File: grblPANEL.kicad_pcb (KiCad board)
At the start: 4 copper layers, 84 x 55 mm, 122 parts, among them J101 Conn_01x02, J201 2x5x1.27mm, J202 USB_C_Receptacle_USB2.0, J301 Conn_01x02, J401 Conn_01x02, J501 ILI9488, J601 Conn_02x10_Odd_Even, J701 Conn_01x04, J702 Conn_01x04, J703 Conn_01x04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

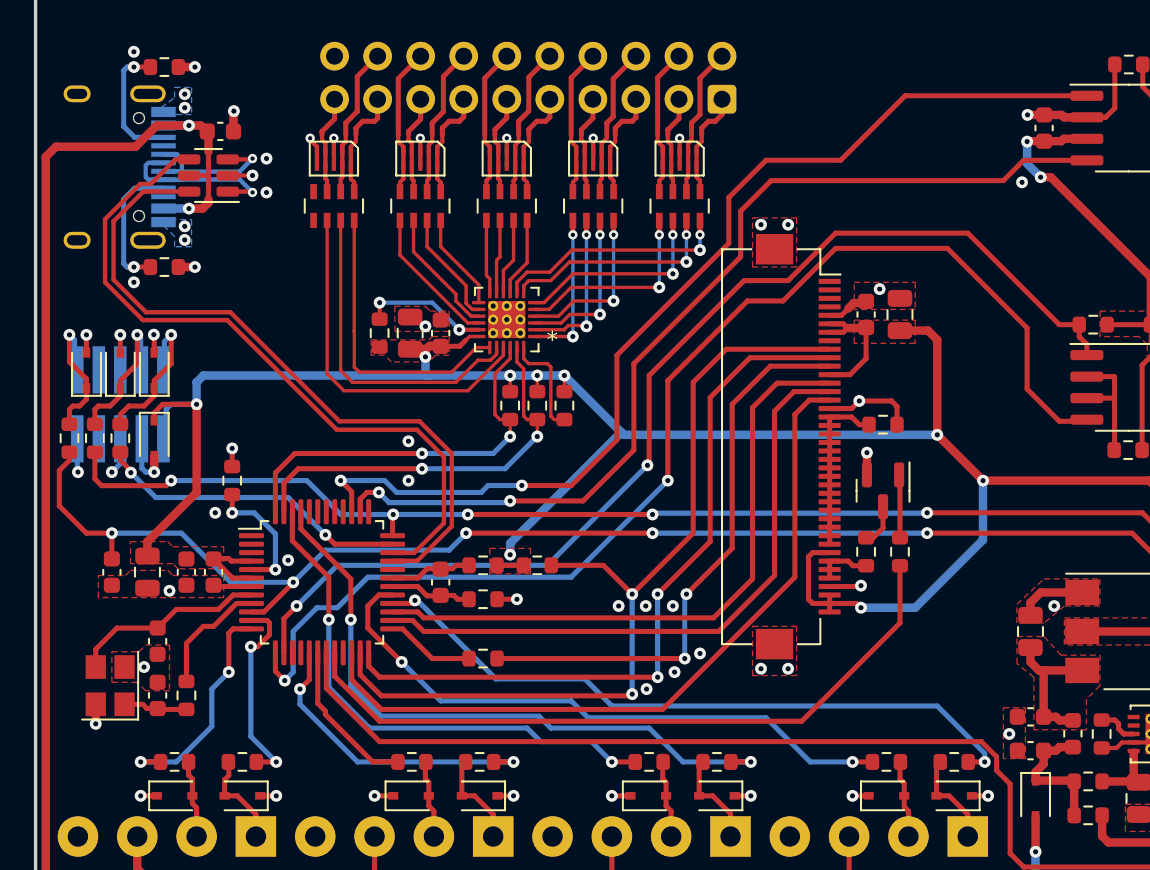
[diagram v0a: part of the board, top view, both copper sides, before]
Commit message: Ensure silkscreen is not covering holes
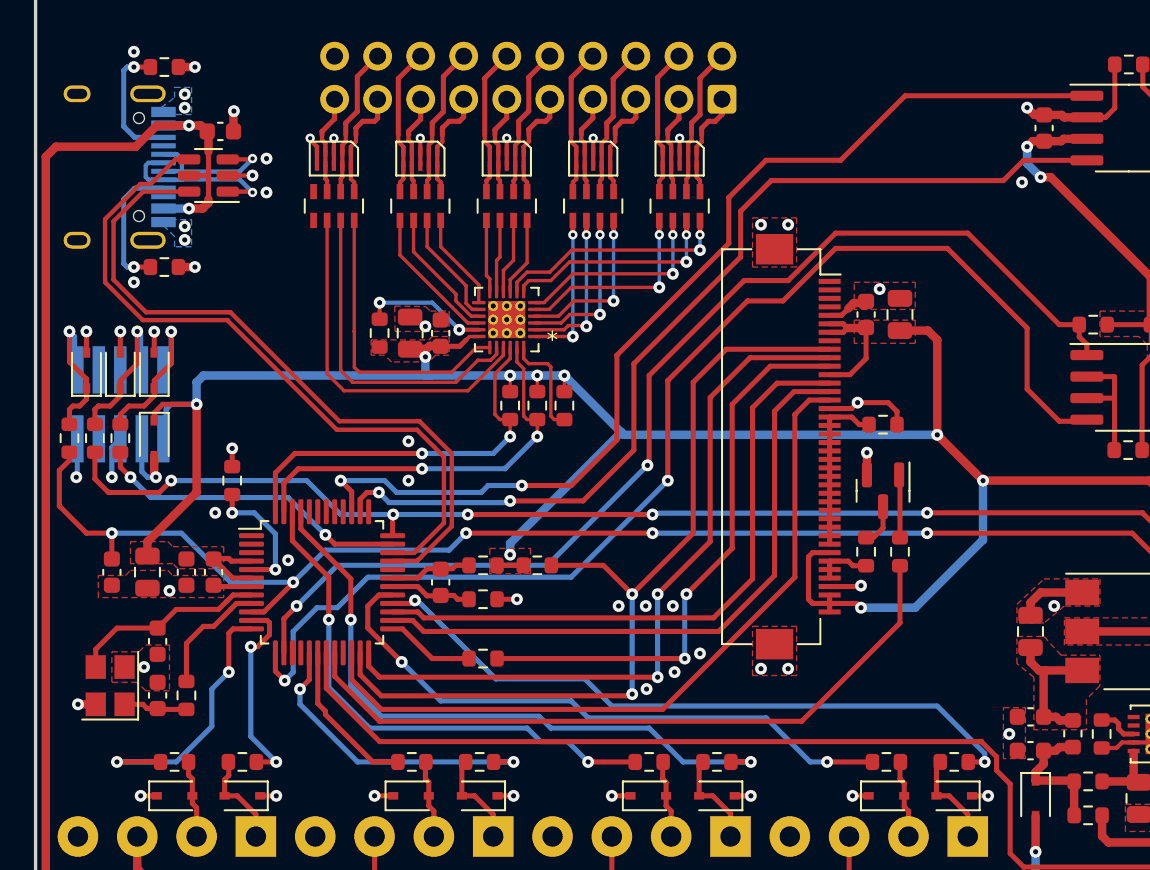
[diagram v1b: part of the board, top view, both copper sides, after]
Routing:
- net ENCODER_4_B: track 13.6 -> 16.4 mm
- net GND: track 91.8 -> 93.6 mm

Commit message: small cleanups
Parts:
- RN601, RN602, RN603, RN604, RN605: footprint Resistor_SMD:R_Array_Concave_4x0603 -> Resistor_SMD:R_Array_Convex_4x0603
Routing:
- net GND: track 93.6 -> 92.8 mm

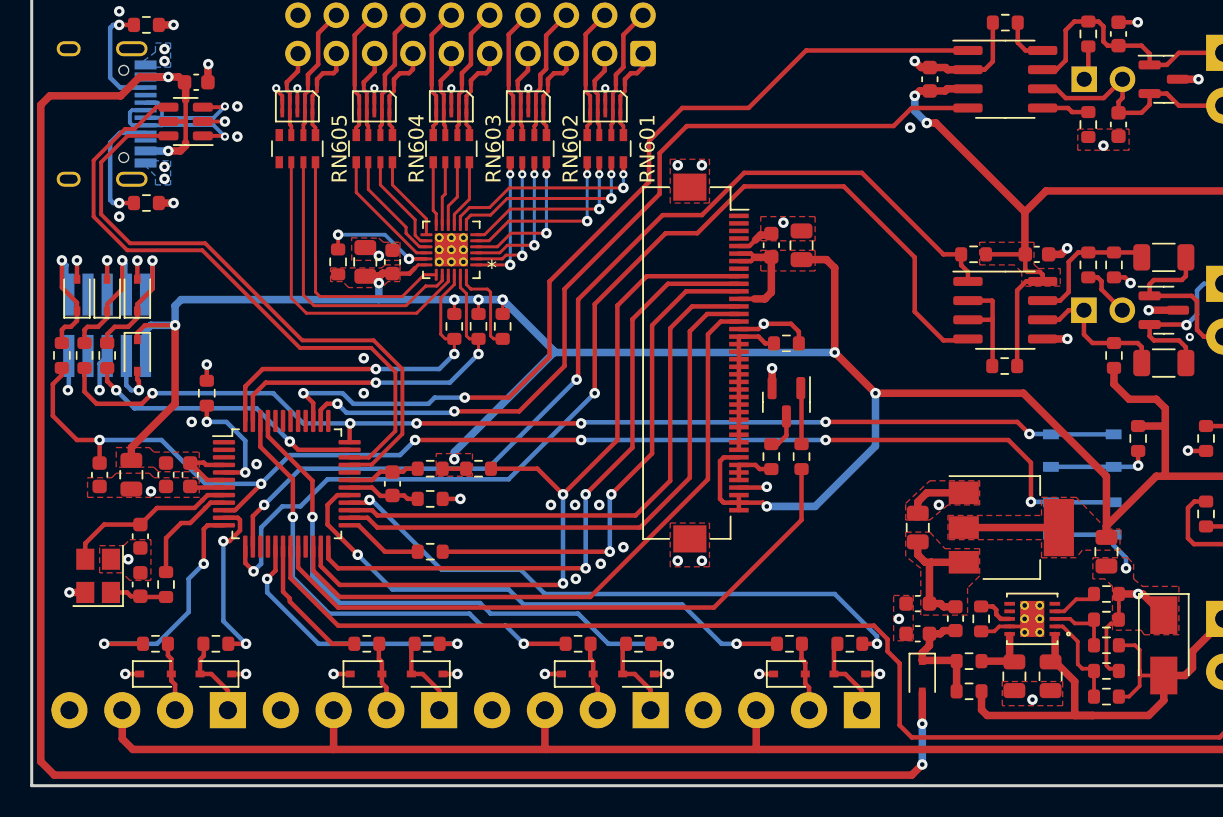
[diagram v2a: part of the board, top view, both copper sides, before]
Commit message: place gnd vias near all signal and power vias
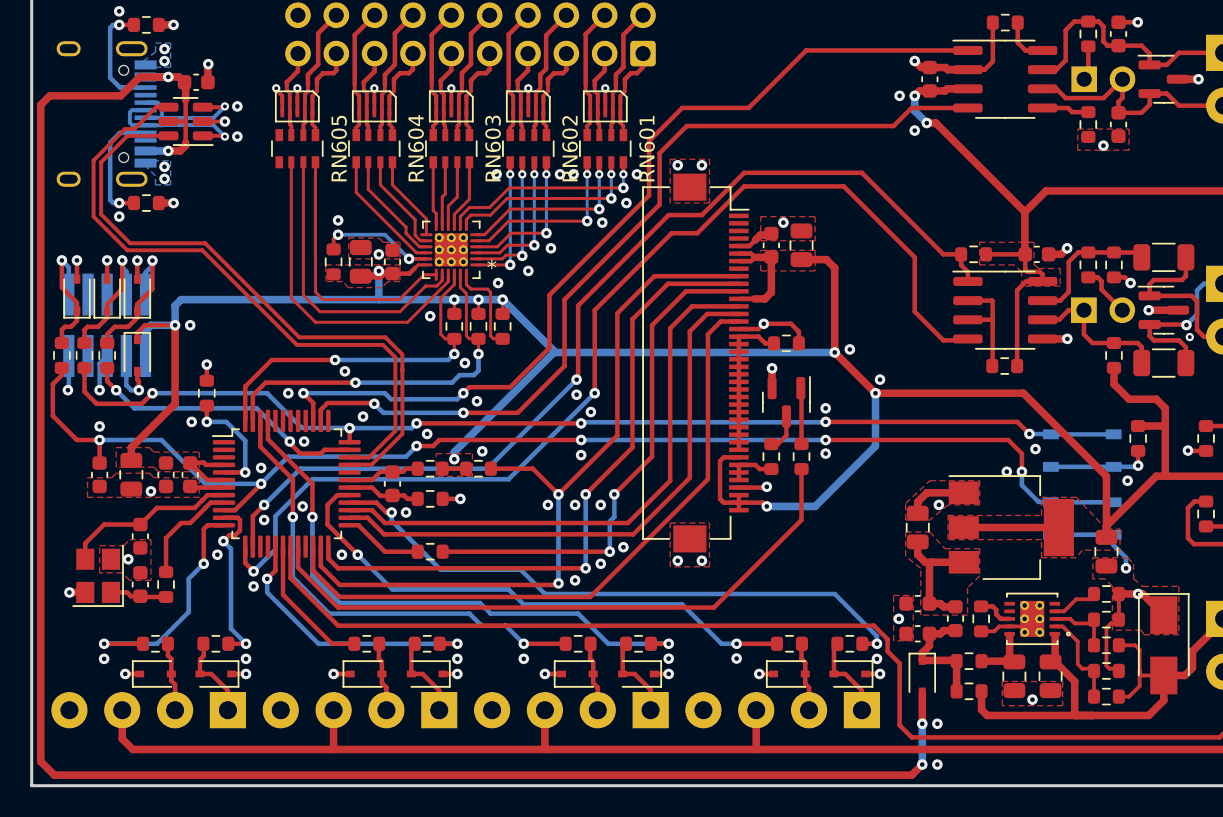
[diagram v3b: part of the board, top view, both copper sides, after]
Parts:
- moved C601 0.30 mm to (42.8, 149.3)
- moved R604 0.30 mm to (41.0, 149.3)
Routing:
- net +3V3: track 354.5 -> 355.3 mm
- net DISPLAY_CS: track 52.1 -> 51.4 mm
- net /MCU/USB_D-: track 41.5 -> 42.2 mm
- net KEYPAD_CLK: track 23.9 -> 24.5 mm
- net CAN_TX: track 60.6 -> 60.0 mm
- net /MCU/USB_D+: track 42.1 -> 42.6 mm
- net GND: vias 72 -> 117

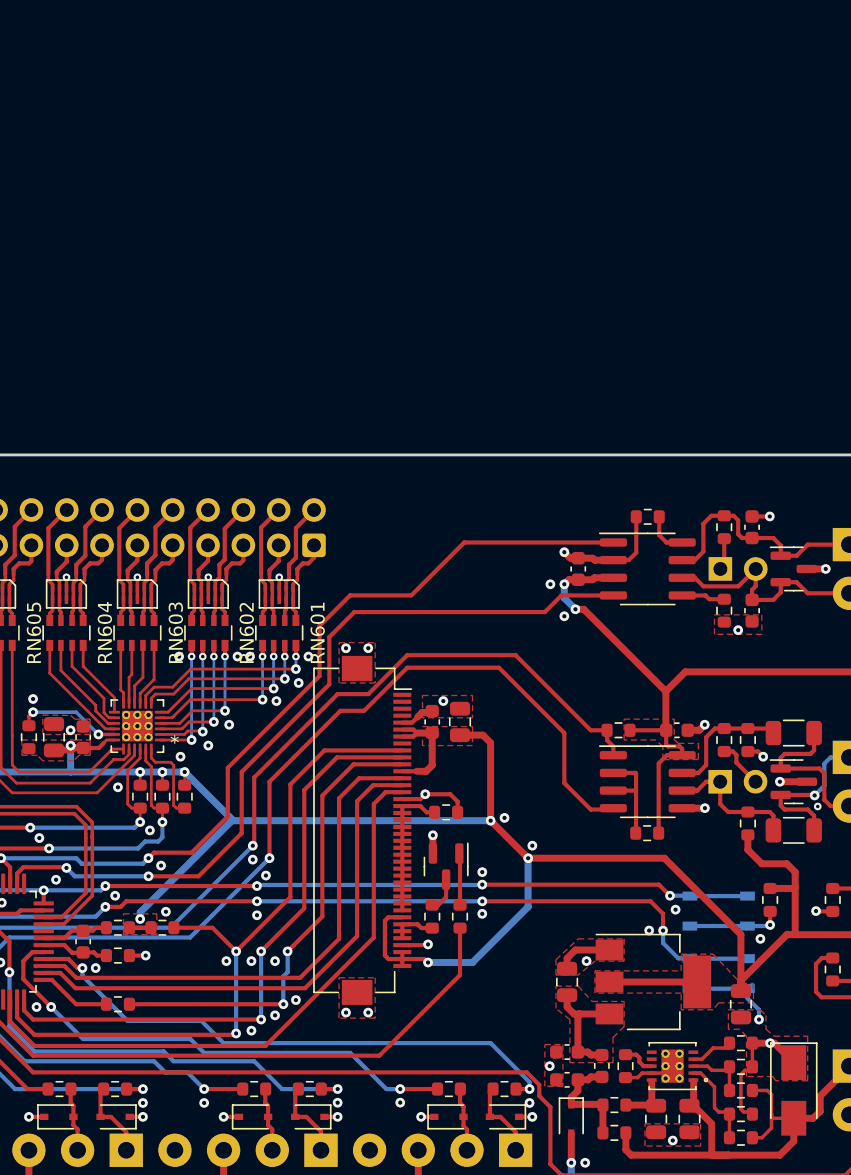
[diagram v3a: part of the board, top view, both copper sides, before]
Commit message: sheet 1 test points
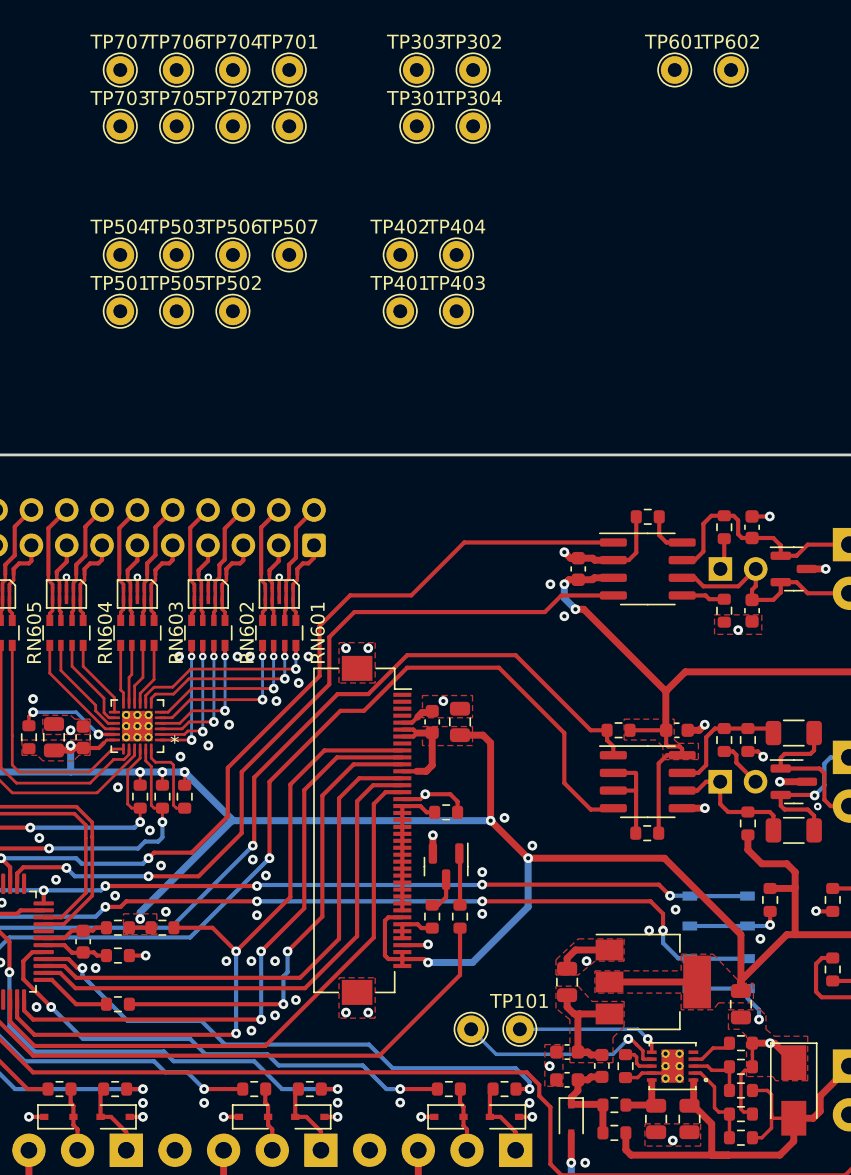
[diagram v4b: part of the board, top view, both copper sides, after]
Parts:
- added TP101: TestPoint, TestPoint:TestPoint_THTPad_D2.0mm_Drill1.0mm, F.Cu at (76.3, 170.3)
- added TP102: TestPoint, TestPoint:TestPoint_THTPad_D2.0mm_Drill1.0mm, F.Cu at (72.8, 170.3)
- added TP301: TestPoint, TestPoint:TestPoint_THTPad_D2.0mm_Drill1.0mm, F.Cu at (68.9, 105.4)
- added TP302: TestPoint, TestPoint:TestPoint_THTPad_D2.0mm_Drill1.0mm, F.Cu at (72.9, 101.3)
- added TP303: TestPoint, TestPoint:TestPoint_THTPad_D2.0mm_Drill1.0mm, F.Cu at (68.9, 101.3)
- added TP304: TestPoint, TestPoint:TestPoint_THTPad_D2.0mm_Drill1.0mm, F.Cu at (72.9, 105.4)
- added TP401: TestPoint, TestPoint:TestPoint_THTPad_D2.0mm_Drill1.0mm, F.Cu at (67.7, 118.7)
- added TP402: TestPoint, TestPoint:TestPoint_THTPad_D2.0mm_Drill1.0mm, F.Cu at (67.7, 114.6)
- added TP403: TestPoint, TestPoint:TestPoint_THTPad_D2.0mm_Drill1.0mm, F.Cu at (71.8, 118.7)
- added TP404: TestPoint, TestPoint:TestPoint_THTPad_D2.0mm_Drill1.0mm, F.Cu at (71.8, 114.6)
- added TP501: TestPoint, TestPoint:TestPoint_THTPad_D2.0mm_Drill1.0mm, F.Cu at (47.6, 118.7)
- added TP502: TestPoint, TestPoint:TestPoint_THTPad_D2.0mm_Drill1.0mm, F.Cu at (55.7, 118.7)
- added TP503: TestPoint, TestPoint:TestPoint_THTPad_D2.0mm_Drill1.0mm, F.Cu at (51.6, 114.6)
- added TP504: TestPoint, TestPoint:TestPoint_THTPad_D2.0mm_Drill1.0mm, F.Cu at (47.6, 114.6)
- added TP505: TestPoint, TestPoint:TestPoint_THTPad_D2.0mm_Drill1.0mm, F.Cu at (51.6, 118.7)
- added TP506: TestPoint, TestPoint:TestPoint_THTPad_D2.0mm_Drill1.0mm, F.Cu at (55.7, 114.6)
- added TP507: TestPoint, TestPoint:TestPoint_THTPad_D2.0mm_Drill1.0mm, F.Cu at (59.7, 114.6)
- added TP601: TestPoint, TestPoint:TestPoint_THTPad_D2.0mm_Drill1.0mm, F.Cu at (87.4, 101.3)
- added TP602: TestPoint, TestPoint:TestPoint_THTPad_D2.0mm_Drill1.0mm, F.Cu at (91.5, 101.3)
- added TP701: TestPoint, TestPoint:TestPoint_THTPad_D2.0mm_Drill1.0mm, F.Cu at (59.7, 101.3)
- added TP702: TestPoint, TestPoint:TestPoint_THTPad_D2.0mm_Drill1.0mm, F.Cu at (55.7, 105.4)
- added TP703: TestPoint, TestPoint:TestPoint_THTPad_D2.0mm_Drill1.0mm, F.Cu at (47.6, 105.4)
- added TP704: TestPoint, TestPoint:TestPoint_THTPad_D2.0mm_Drill1.0mm, F.Cu at (55.7, 101.3)
- added TP705: TestPoint, TestPoint:TestPoint_THTPad_D2.0mm_Drill1.0mm, F.Cu at (51.6, 105.4)
- added TP706: TestPoint, TestPoint:TestPoint_THTPad_D2.0mm_Drill1.0mm, F.Cu at (51.6, 101.3)
- added TP707: TestPoint, TestPoint:TestPoint_THTPad_D2.0mm_Drill1.0mm, F.Cu at (47.6, 101.3)
- added TP708: TestPoint, TestPoint:TestPoint_THTPad_D2.0mm_Drill1.0mm, F.Cu at (59.7, 105.4)
- C206, C207: value 10p -> 16p
- C302, C303: value 10p -> DNP
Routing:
- net /Power/UVOV: track 0.00 -> 15.1 mm, vias 0 -> 1
- net /Power/FLAG: track 0.00 -> 10.6 mm, vias 0 -> 1

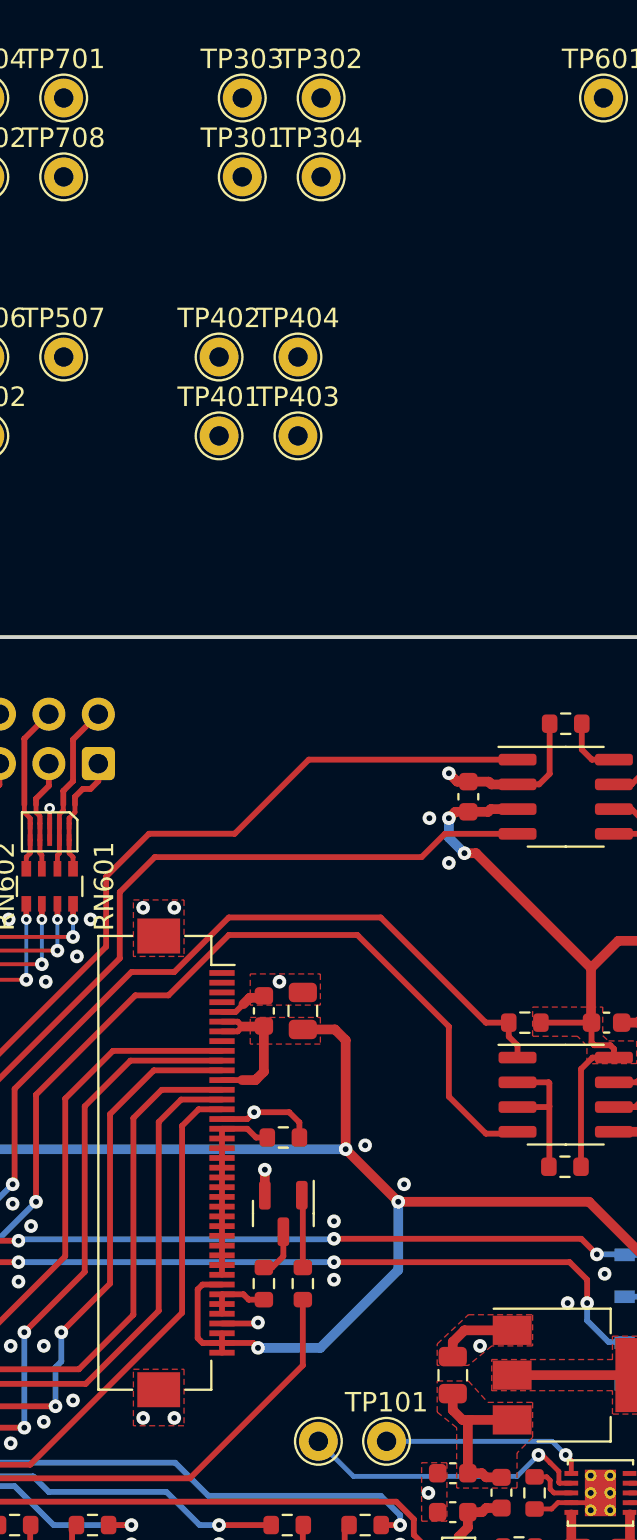
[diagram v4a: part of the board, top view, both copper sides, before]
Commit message: canbus & modbus test points
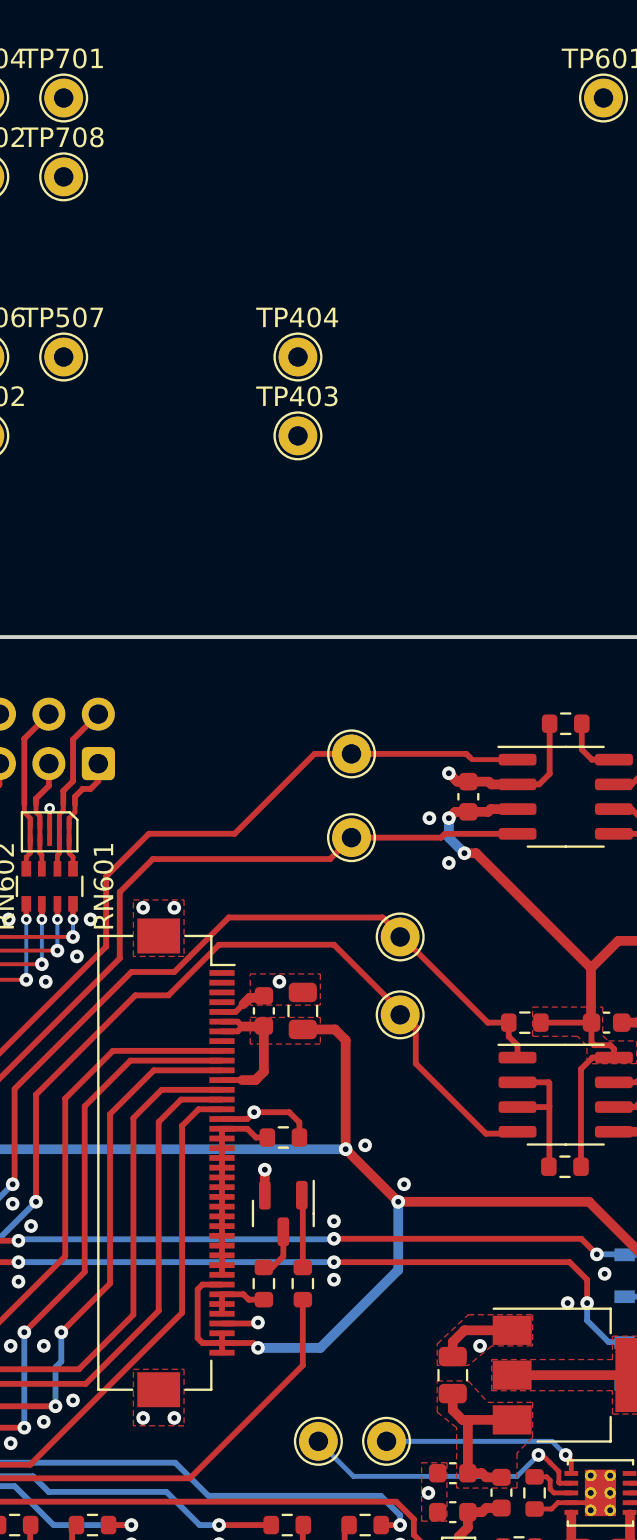
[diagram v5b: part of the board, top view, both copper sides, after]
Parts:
- removed TP303, TP304: TestPoint, TestPoint:TestPoint_THTPad_D2.0mm_Drill1.0mm
- moved TP302 38.0 mm to (74.5, 139.3)
- moved TP402 35.0 mm to (77.0, 148.4)
- moved TP301 30.2 mm to (74.5, 135.0)
- moved TP401 27.4 mm to (77.0, 144.4)
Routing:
- net MODBUS_TX: track 70.5 -> 69.1 mm
